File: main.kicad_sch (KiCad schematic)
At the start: 0 parts

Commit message: Adding in schematic for boost stage
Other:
- added sheet boost_frontend (boost_frontend.kicad_sch)
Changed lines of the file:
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@@
 	(generator_version "9.0")
 	(paper "A4")
+	(sheet
+		(at 116.84 71.12)
+		(size 15.24 17.78)
+		(exclude_from_sim no)
+		(in_bom yes)
+		(on_board yes)
+		(dnp no)
+		(fields_autoplaced yes)
+		(stroke
+			(width 0.1524)
+			(type solid)
+		)
+		(fill
+			(color 0 0 0 0.0000)
+		)
+		(property "Sheetname" "boost_frontend"
+			(at 116.84 70.4084 0)
+			(effects
+				(font
+					(size 1.27 1.27)
+				)
+				(justify left bottom)
+			)
+		)
+		(property "Sheetfile" "boost_frontend.kicad_sch"
+			(at 116.84 89.4846 0)
+			(effects
+				(font
+					(size 1.27 1.27)
+				)
+				(justify left top)
+			)
+		)
+		(instances
+			(project "PowerBoard"
+				(path "/99785679-20de-4827-b4cc-bc3c187068c9/9564929a-642e-4163-88c2-45054b63a5ed"
+					(page "4")
+				)
+			)
+		)
+	)
 )

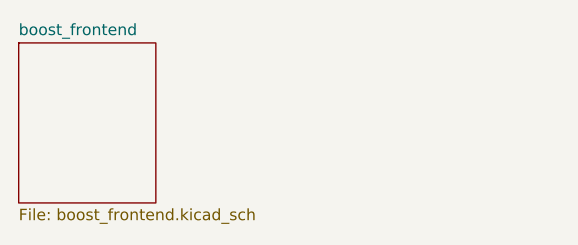
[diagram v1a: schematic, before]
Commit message: Adding passives to boost stage
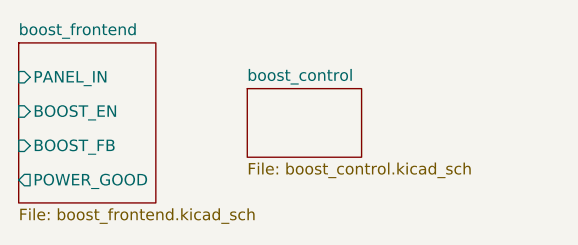
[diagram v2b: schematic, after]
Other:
- added sheet boost_control (boost_control.kicad_sch)
- sheet boost_frontend ports: added BOOST_EN, BOOST_FB, PANEL_IN, POWER_GOOD; removed none
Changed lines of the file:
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@@
 	(paper "A4")
+	(sheet
+		(at 142.24 76.2)
+		(size 12.7 7.62)
+		(exclude_from_sim no)
+		(in_bom yes)
+		(on_board yes)
+		(dnp no)
+		(fields_autoplaced yes)
+		(stroke
+			(width 0.1524)
+			(type solid)
+		)
+		(fill
+			(color 0 0 0 0.0000)
+		)
+		(property "Sheetname" "boost_control"
+			(at 142.24 75.4884 0)
+			(effects
+				(font
+					(size 1.27 1.27)
+				)
+				(justify left bottom)
+			)
+		)
+		(property "Sheetfile" "boost_control.kicad_sch"
+			(at 142.24 84.4046 0)
+			(effects
+				(font
+					(size 1.27 1.27)
+				)
+				(justify left top)
+			)
+		)
+		(instances
+			(project "PowerBoard"
+				(path "/99785679-20de-4827-b4cc-bc3c187068c9/9564929a-642e-4163-88c2-45054b63a5ed"
+					(page "5")
+				)
+			)
+		)
+	)
 	(sheet
 		(at 116.84 71.12)
@@
 			)
 		)
+		(pin "PANEL_IN" input
+			(at 116.84 74.93 180)
+			(effects
+				(font
+					(size 1.27 1.27)
+				)
+				(justify left)
+			)
+		)
+		(pin "BOOST_EN" input
+			(at 116.84 78.74 180)
+			(effects
+				(font
+					(size 1.27 1.27)
+				)
+				(justify left)
+			)
+		)
+		(pin "BOOST_FB" input
+			(at 116.84 82.55 180)
+			(effects
+				(font
+					(size 1.27 1.27)
+				)
+				(justify left)
+			)
+		)
+		(pin "POWER_GOOD" output
+			(at 116.84 86.36 180)
+			(effects
+				(font
+					(size 1.27 1.27)
+				)
+				(justify left)
+			)
+		)

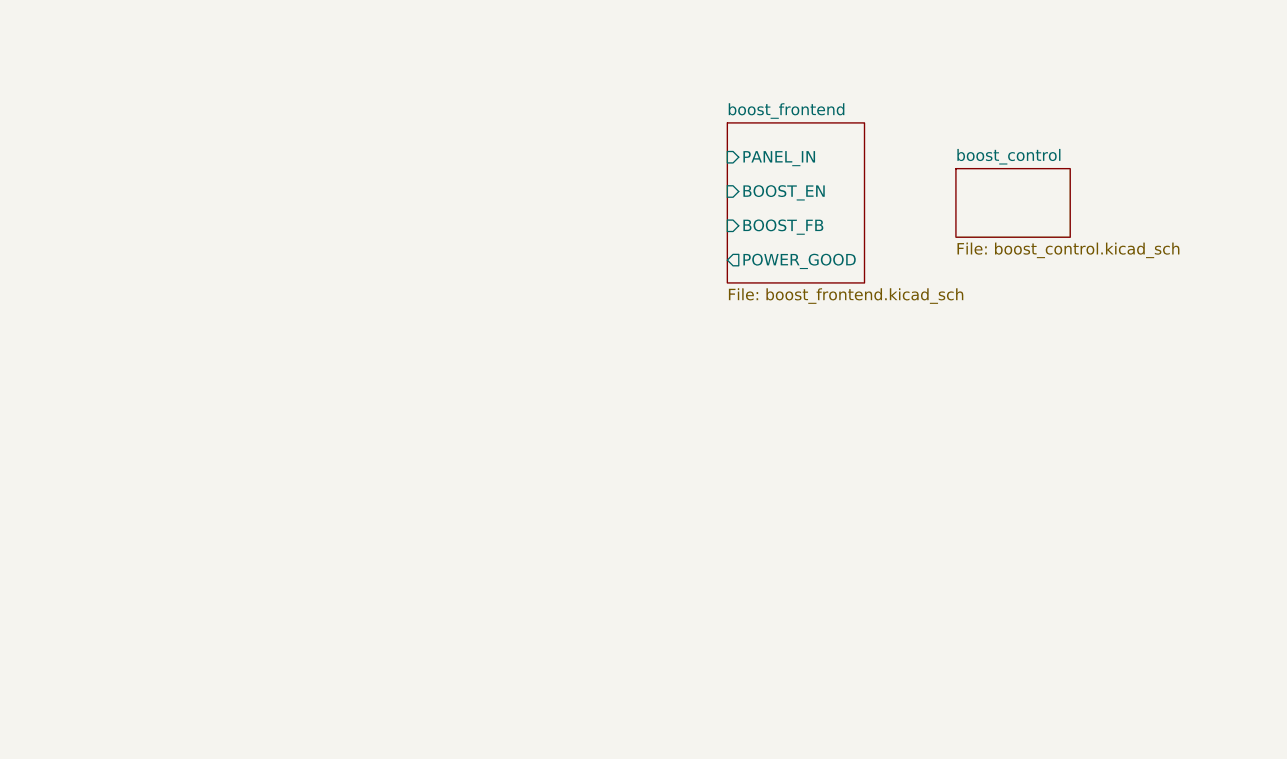
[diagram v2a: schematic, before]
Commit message: Adding hierarchical sheets for other parts of circuit
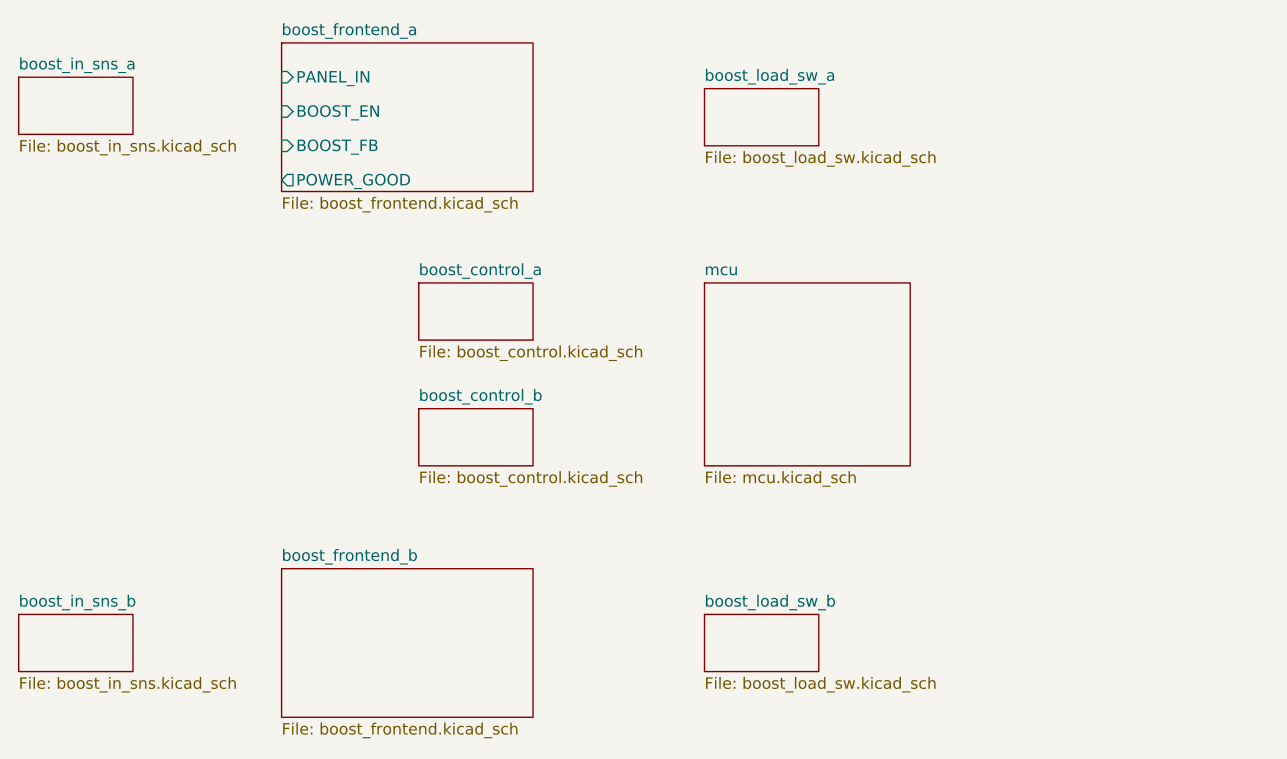
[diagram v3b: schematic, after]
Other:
- sheet boost_control renamed boost_control_a
- sheet boost_frontend renamed boost_frontend_a
- added sheet boost_control_b (boost_control.kicad_sch)
- added sheet boost_frontend_b (boost_frontend.kicad_sch)
- added sheet boost_in_sns_a (boost_in_sns.kicad_sch)
- added sheet boost_in_sns_b (boost_in_sns.kicad_sch)
- added sheet boost_load_sw_a (boost_load_sw.kicad_sch)
- added sheet boost_load_sw_b (boost_load_sw.kicad_sch)
- added sheet mcu (mcu.kicad_sch)

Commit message: Working on power board
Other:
- added sheet solar_panels (solar_panels.kicad_sch)
- sheet boost_control_a ports: added FB_OUT, I2C; removed none
- sheet boost_control_b ports: added FB_OUT, I2C; removed none
- sheet boost_frontend_a ports: added BOOST_OUT, BOOST_SIG; removed BOOST_EN, POWER_GOOD
- sheet boost_frontend_b ports: added BOOST_FB, BOOST_OUT, BOOST_SIG, PANEL_IN; removed none
- sheet boost_in_sns_a ports: added I2C, PANEL_DRV, PANEL_IN, PANEL_IN_ALERT; removed none
- sheet boost_in_sns_b ports: added I2C, PANEL_DRV, PANEL_IN, PANEL_IN_ALERT; removed none
- sheet boost_load_sw_a ports: added BOOST_IN, VBUS; removed none
- sheet boost_load_sw_b ports: added BOOST_IN, VBUS; removed none
- sheet mcu ports: added BOOST_A_SIG, BOOST_B_SIG, I2C; removed none

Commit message: Adding more schematic blocks
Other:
- added sheet backup_batt_load_sw (boost_load_sw.kicad_sch)
- added sheet batt1_load_sw (boost_load_sw.kicad_sch)
- added sheet batt2_load_sw (boost_load_sw.kicad_sch)
- added sheet output (output_connectors.kicad_sch)
- sheet boost_in_sns_a ports: added IN, OUT; removed PANEL_DRV, PANEL_IN
- sheet boost_in_sns_b ports: added IN, OUT; removed PANEL_DRV, PANEL_IN
- sheet boost_load_sw_a ports: added IN, OUT; removed BOOST_IN, VBUS
- sheet boost_load_sw_b ports: added IN, OUT; removed BOOST_IN, VBUS

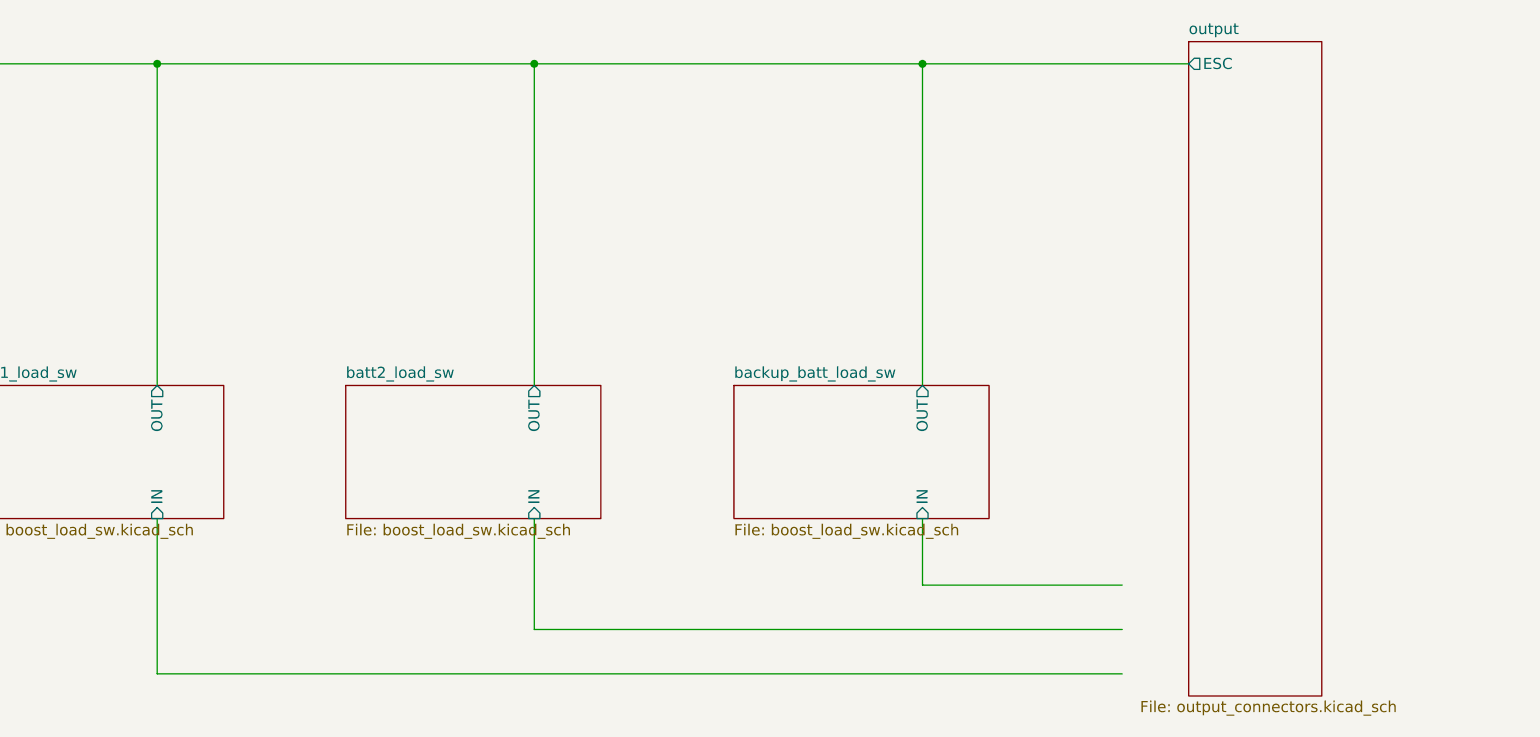
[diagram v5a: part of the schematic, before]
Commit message: Working on load switches
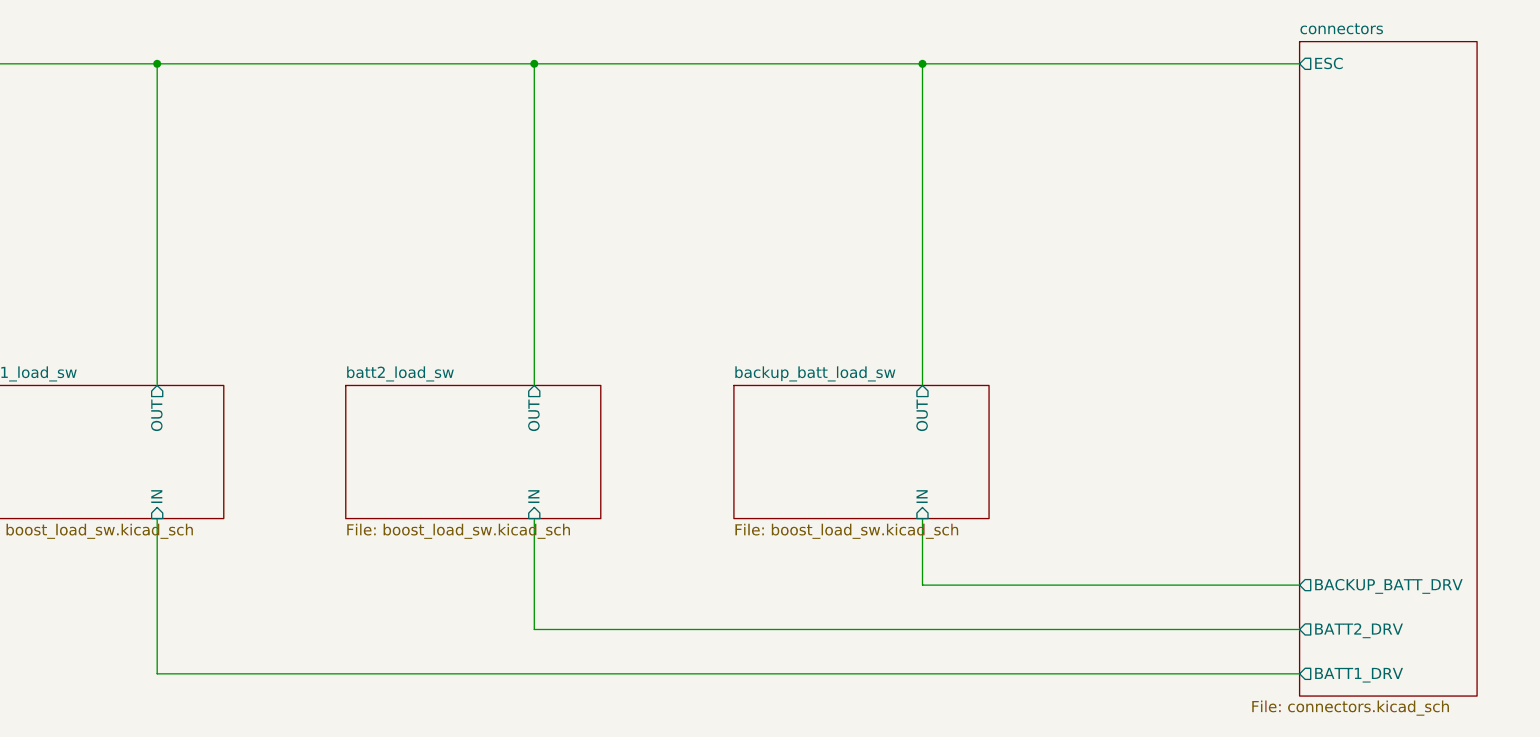
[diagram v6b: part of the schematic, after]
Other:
- sheet output renamed connectors
- sheet connectors: file output_connectors.kicad_sch -> connectors.kicad_sch
- sheet connectors ports: added BACKUP_BATT_DRV, BATT1_DRV, BATT2_DRV; removed none
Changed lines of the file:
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@@
 	(wire
 		(pts
-			(xy 287.02 171.45) (xy 354.33 171.45)
-		)
-		(stroke
-			(width 0)
-			(type default)
-		)
-	)
-	(wire
-		(pts
-			(xy 331.47 106.68) (xy 361.95 106.68)
+			(xy 287.02 171.45) (xy 374.65 171.45)
+		)
+		(stroke
+			(width 0)
+			(type default)
+		)
+	)
+	(wire
+		(pts
+			(xy 331.47 106.68) (xy 374.65 106.68)
 		)
 		(stroke
@@
 			(width 0)
 			(type default)
+			(color 0 0 194 1)
 		)
 	)
@@
 			(width 0)
 			(type default)
-		)
-	)
-	(wire
-		(pts
-			(xy 331.47 166.37) (xy 354.33 166.37)
+			(color 0 0 194 1)
+		)
+	)
+	(wire
+		(pts
+			(xy 331.47 166.37) (xy 374.65 166.37)
 		)
 		(stroke
@@
 			(width 0)
 			(type default)
+			(color 0 194 0 1)
 		)
 	)
@@
 	(wire
 		(pts
-			(xy 243.84 176.53) (xy 354.33 176.53)
+			(xy 243.84 176.53) (xy 374.65 176.53)
 		)
 		(stroke
@@
 			(width 0)
 			(type default)
+			(color 0 194 0 1)
 		)
 	)
@@
 			(width 0)
 			(type default)
+			(color 0 194 0 1)
 		)
 	)
@@
 			(width 0)
 			(type default)
+			(color 0 0 194 1)
 		)
 	)
@@
 		(polyline
 			(pts
-				(xy 204.47 177.8) (xy 204.47 104.14) (xy 212.09 104.14) (xy 212.09 177.8)
+				(xy 353.06 177.8) (xy 353.06 104.14) (xy 356.87 104.14) (xy 356.87 177.8)
 			)
 			(stroke
@@
 		(length 2.54)
 		(shape round)
-		(at 208.28 104.14 0)
+		(at 355.6 104.14 0)
 		(fields_autoplaced yes)
 		(effects
@@
 		)
 		(property "Netclass" "cls_HPBUS"
-			(at 208.9785 101.6 0)
+			(at 356.2985 101.6 0)
 			(effects
 				(font
@@
 		)
 		(property "Component Class" ""
-			(at 62.23 57.15 0)
+			(at 209.55 57.15 0)
 			(effects
 				(font
@@
 	)
 	(sheet
-		(at 361.95 104.14)
-		(size 15.24 74.93)
+		(at 374.65 104.14)
+		(size 20.32 74.93)
 		(exclude_from_sim no)
 		(in_bom yes)
@@
 			(color 0 0 0 0.0000)
 		)
-		(property "Sheetname" "output"
-			(at 361.95 103.4284 0)
+		(property "Sheetname" "connectors"
+			(at 374.65 103.4284 0)
 			(effects
 				(font
@@
 			)
 		)
-		(property "Sheetfile" "output_connectors.kicad_sch"
-			(at 356.362 179.578 0)
+		(property "Sheetfile" "connectors.kicad_sch"
+			(at 369.062 179.578 0)
 			(effects
 				(font
@@
 		)
 		(pin "ESC" output
-			(at 361.95 106.68 180)
-			(effects
-				(font
+			(at 374.65 106.68 180)
+			(effects
+				(font
+					(size 1.27 1.27)
+				)
+				(justify left)
+			)
+		)
+		(pin "BACKUP_BATT_DRV" output
+			(at 374.65 166.37 180)
+			(effects
+				(font
+					(size 1.27 1.27)
+				)
+				(justify left)
+			)
+		)
+		(pin "BATT1_DRV" output
+			(at 374.65 176.53 180)
+			(effects
+				(font
+					(size 1.27 1.27)
+				)
+				(justify left)
+			)
+		)
+		(pin "BATT2_DRV" output
+			(at 374.65 171.45 180)
+			(effects
+				(font

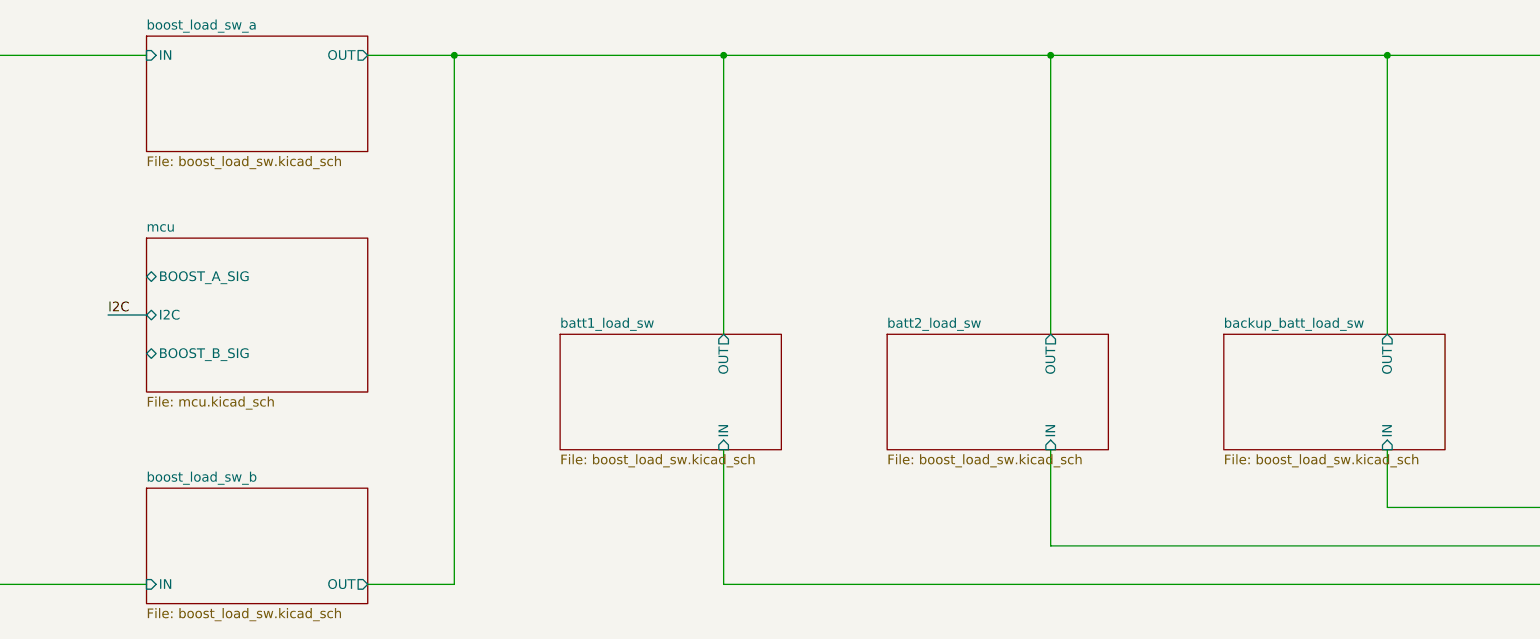
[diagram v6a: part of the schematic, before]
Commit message: Working on load switch design
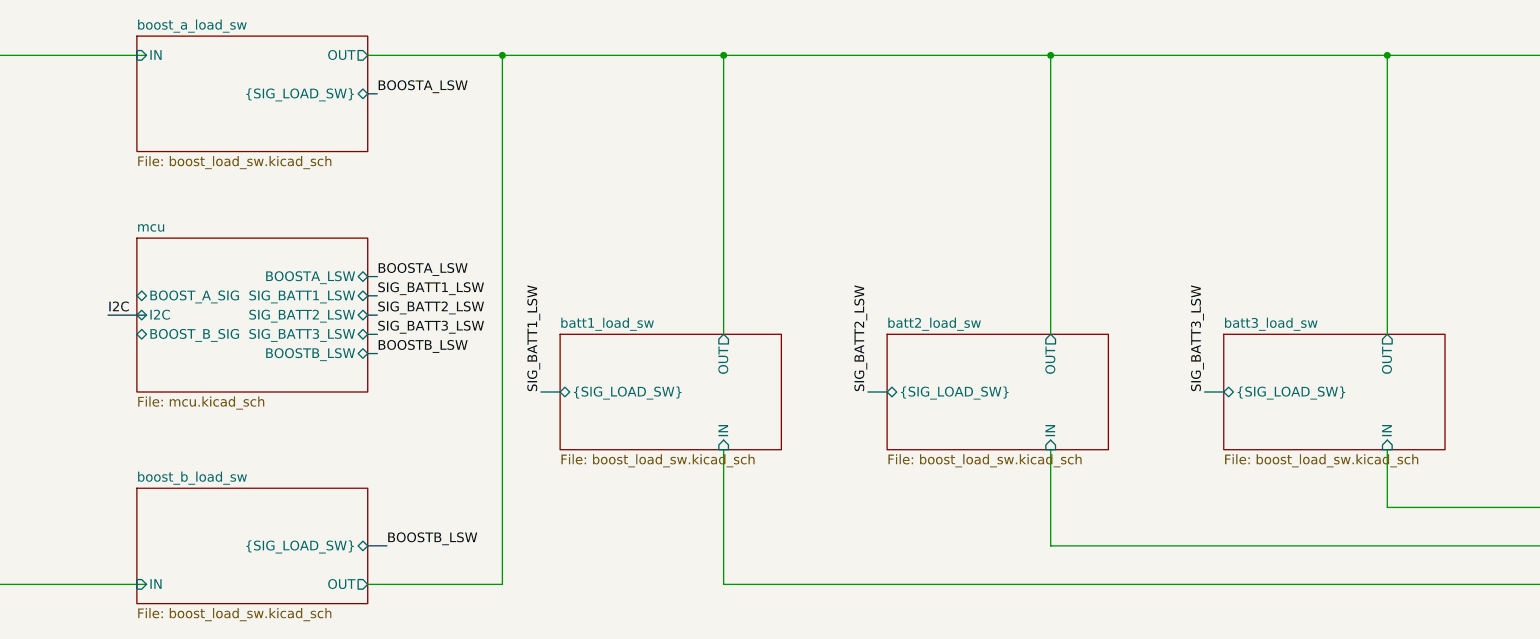
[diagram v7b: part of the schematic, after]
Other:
- sheet backup_batt_load_sw renamed batt3_load_sw
- sheet boost_load_sw_a renamed boost_a_load_sw
- sheet boost_load_sw_b renamed boost_b_load_sw
- sheet batt1_load_sw ports: added {SIG_LOAD_SW}; removed none
- sheet batt2_load_sw ports: added {SIG_LOAD_SW}; removed none
- sheet batt3_load_sw ports: added {SIG_LOAD_SW}; removed none
- sheet boost_a_load_sw ports: added {SIG_LOAD_SW}; removed none
- sheet boost_b_load_sw ports: added {SIG_LOAD_SW}; removed none
- sheet mcu ports: added BOOSTA_LSW, BOOSTB_LSW, SIG_BATT1_LSW, SIG_BATT2_LSW, SIG_BATT3_LSW; removed none

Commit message: Working on 5v supply
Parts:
- added R69, R70: R_US, symbol Device:R_US
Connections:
- new net GND: R69.1, R70.2
- new net SCL: R70.1
- new net SDA: R69.2
- no-connect marks 0 -> 2
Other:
- sheet boost_frontend_a renamed boost_a_frontend
- sheet boost_frontend_b renamed boost_b_frontend
- sheet boost_in_sns_a renamed boost_b_in_sns
- removed sheet boost_in_sns_b
- added sheet housekeeping (housekeeping.kicad_sch)
- sheet batt1_load_sw: file boost_load_sw.kicad_sch -> load_sw.kicad_sch
- sheet batt2_load_sw: file boost_load_sw.kicad_sch -> load_sw.kicad_sch
- sheet batt3_load_sw: file boost_load_sw.kicad_sch -> load_sw.kicad_sch
- sheet boost_a_frontend ports: added {SIG_BOOST}; removed BOOST_FB, BOOST_SIG
- sheet boost_a_load_sw: file boost_load_sw.kicad_sch -> load_sw.kicad_sch
- sheet boost_b_frontend ports: added {SIG_BOOST}; removed BOOST_FB, BOOST_SIG
- sheet boost_b_in_sns: file boost_in_sns.kicad_sch -> power_sns.kicad_sch
- sheet boost_b_load_sw: file boost_load_sw.kicad_sch -> load_sw.kicad_sch
- sheet boost_control_a ports: added none; removed FB_OUT
- sheet boost_control_b ports: added none; removed FB_OUT
